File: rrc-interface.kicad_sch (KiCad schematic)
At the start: 39 parts, among them J1 Mic Input, J10 Input Only Pins, J11 Input Only Pins, J12 Flash mode, J2 8P8C_LED_Shielded, J3 6P6C RRC, J4 Audio Out, J5 Ptt, J6 TF Set, J7 UART2 Socket, J8 UART Socket, J9 SPI Breakout, U1 ESP32-DevKitC

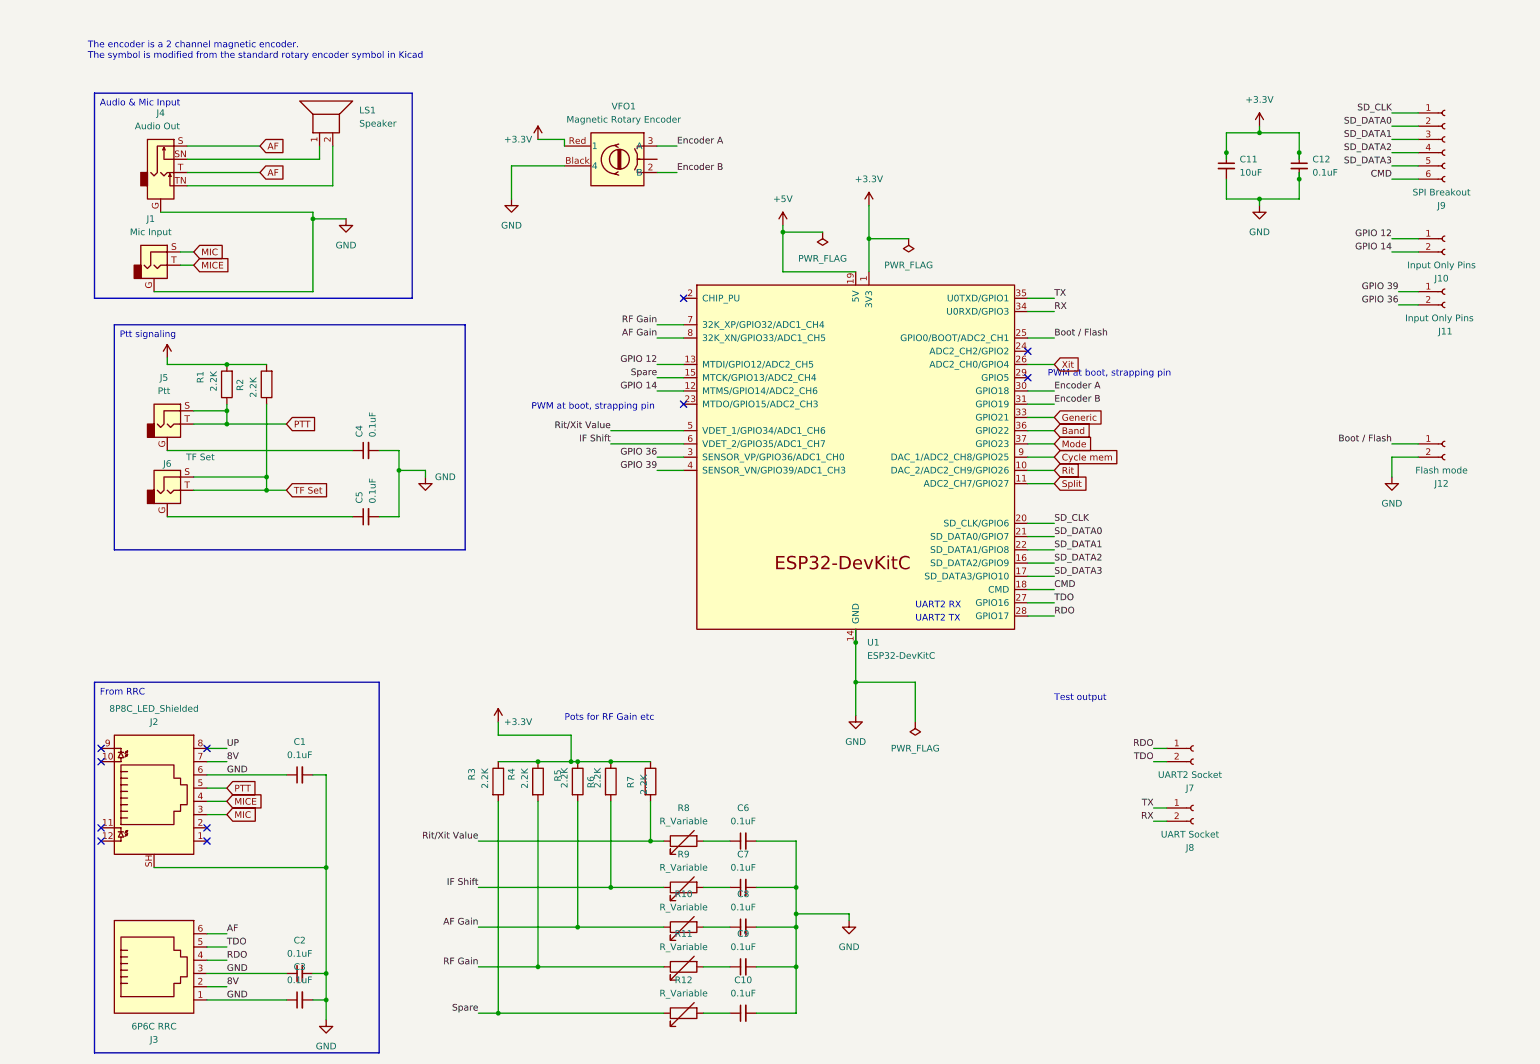
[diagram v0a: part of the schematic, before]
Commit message: cont routing work
Changes:

* Added mounting holes
* Tried to trim down PCB size a litle more.
* Attempted to separate digital IO from analog.
* Added socket IC for RJ45 & 6P6C / RJ12 configurability.
* WIP: Add muxer for UART line switching.

Comment:

The muxer UART functionality isn't complete, the idea is to allow switching between using
the RJ45 RXD & TXD UART to the RJ12 / 6P6C UART lines.
Since the real rrc hardware supports this (depends on the radio configured) & maybe depending on socket strapping..
Need to add a jumper to enable switching between these, alternatively use a GPIO pin??
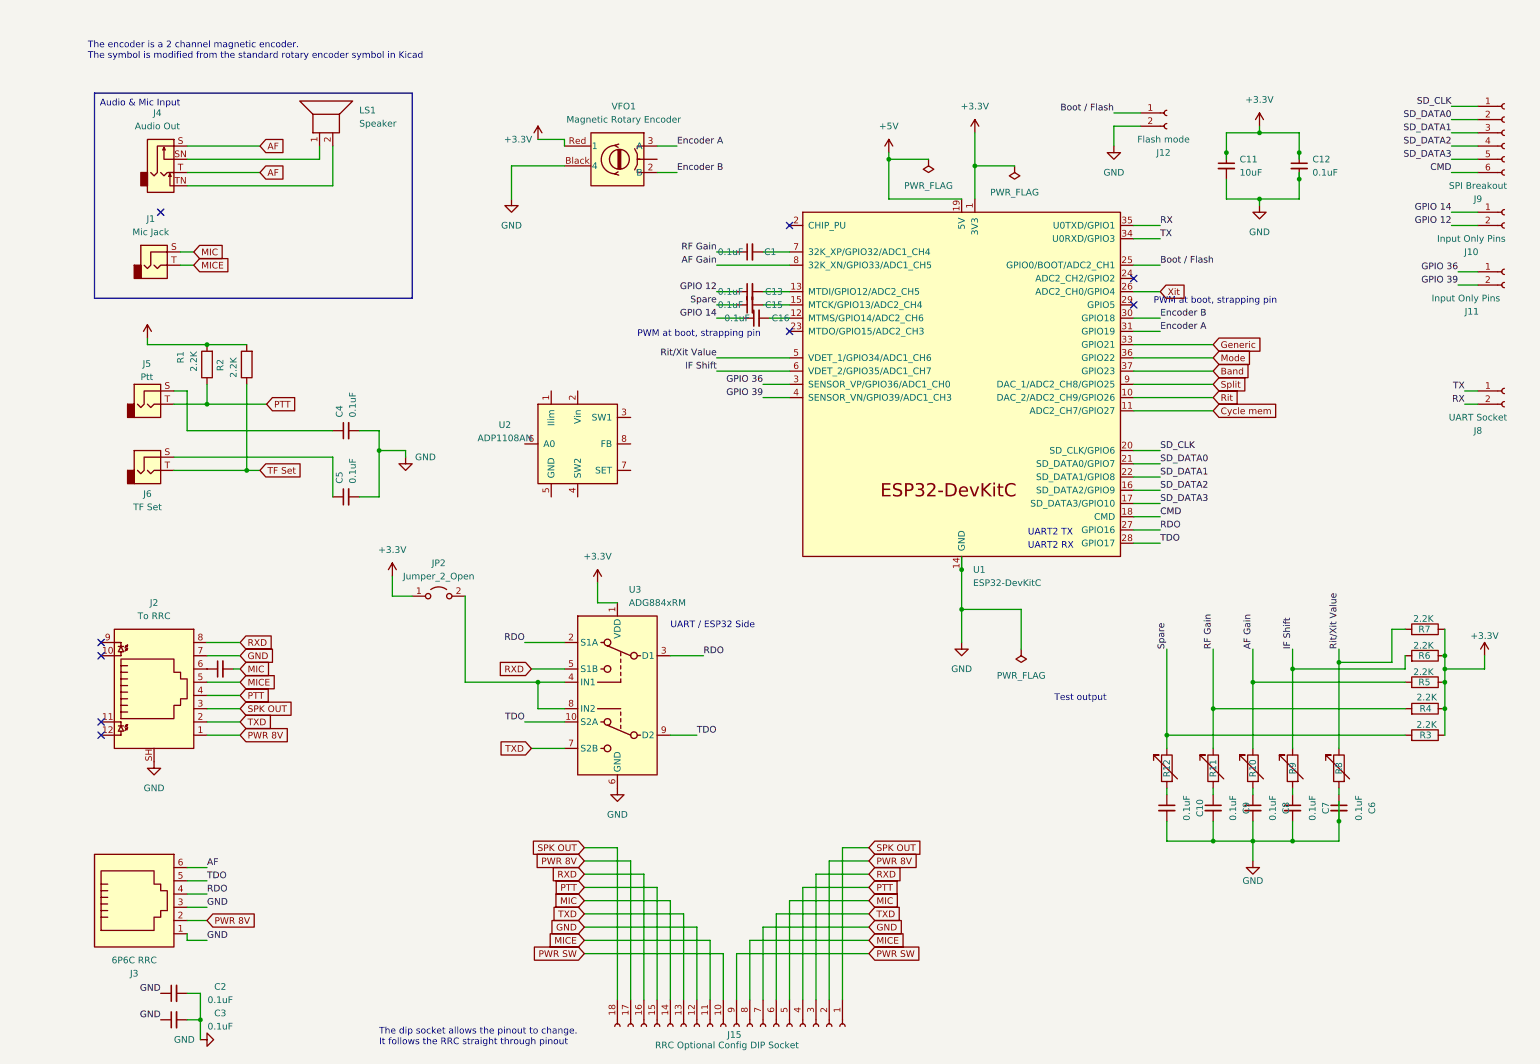
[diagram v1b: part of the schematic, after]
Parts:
- removed J1: Mic Input, Connector_Audio:Jack_3.5mm_CUI_SJ1-3533NG_Horizontal, symbol Connector_Audio:AudioJack2_Ground
- removed J4: Audio Out, Connector_Audio:Jack_3.5mm_CUI_SJ1-3535NG_Horizontal, symbol Connector_Audio:AudioJack2_Ground_Switch
- removed J5: Ptt, Connector_Audio:Jack_3.5mm_CUI_SJ1-3533NG_Horizontal, symbol Connector_Audio:AudioJack2_Ground
- removed J6: TF Set, Connector_Audio:Jack_3.5mm_CUI_SJ1-3533NG_Horizontal, symbol Connector_Audio:AudioJack2_Ground
- removed J7: UART2 Socket, Connector_Molex:Molex_KK-254_AE-6410-02A_1x02_P2.54mm_Vertical, symbol Connector:Conn_01x02_Socket
- added C13, C14, C15, C16: 0.1uF, Capacitor_SMD:C_0603_1608Metric, symbol Device:C_Small
- added J1: Mic Jack, Connector_Audio:Jack_3.5mm_CUI_SJ1-3523N_Horizontal, symbol Connector_Audio:AudioJack2
- added J15: RRC Optional Config DIP Socket, Package_DIP:DIP-18_W7.62mm_Socket, symbol Connector:Conn_01x18_Socket
- added J4: Audio Out, Connector_Audio:Jack_3.5mm_CUI_SJ1-3535NG_Horizontal, symbol Connector_Audio:AudioJack2_Switch
- added J5: Ptt, Connector_Audio:Jack_3.5mm_CUI_SJ1-3523N_Horizontal, symbol Connector_Audio:AudioJack2
- added J6: TF Set, Connector_Audio:Jack_3.5mm_CUI_SJ1-3523N_Horizontal, symbol Connector_Audio:AudioJack2
- added JP2: Jumper_2_Open, symbol Jumper:Jumper_2_Open
- added U2: ADP1108AN, Package_DIP:DIP-8_W7.62mm, symbol Regulator_Switching:ADP1108AN
- added U3: ADG884xRM, Package_SO:MSOP-10_3x3mm_P0.5mm, symbol Analog_Switch:ADG884xRM
- J2: value 8P8C_LED_Shielded -> To RRC
- J9: footprint Connector_Molex:Molex_KK-254_AE-6410-06A_1x06_P2.54mm_Vertical -> Connector_PinSocket_2.54mm:PinSocket_1x06_P2.54mm_Vertical
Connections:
- net +3V3: now also JP2.1 (A), U3.1 (VDD)
- net AF: now also J4.S, J4.T
- net Band: now also U1.37 (GPIO23); no longer U1.36 (GPIO22)
- net Cycle mem: now also U1.11 (ADC2_CH7/GPIO27); no longer U1.9 (DAC_1/ADC2_CH8/GPIO25)
- net Encoder A: now also U1.31 (GPIO19); no longer U1.30 (GPIO18)
- net Encoder B: now also U1.30 (GPIO18); no longer U1.31 (GPIO19)
- net GND: now also J2.7, J15.12 (GND), J15.7 (GND), U3.6 (GND); no longer C1.1, C1.2, J2.6
- net GPIO 12: now also J10.2 (Pin_2), C13.1; no longer J10.1 (Pin_1), U1.13 (MTDI/GPIO12/ADC2_CH5)
- net GPIO 14: now also J10.1 (Pin_1), C16.1; no longer J10.2 (Pin_2), U1.12 (MTMS/GPIO14/ADC2_CH6)
- net GPIO 36: now also J11.1 (Pin_1); no longer J11.2 (Pin_2)
- net GPIO 39: now also J11.2 (Pin_2); no longer J11.1 (Pin_1)
- net MIC: now also C14.2, J1.S, J15.14 (MIC), J15.5 (MIC); no longer J2.3
- net MICE: now also J2.5, J1.T, J15.11 (MICE), J15.8 (MICE); no longer J2.4
- net Mode: now also U1.36 (GPIO22); no longer U1.37 (GPIO23)
- net PTT: now also J2.4, J15.15 (PWR_ON_SW), J15.4 (PWR_ON_SW), J5.T; no longer J2.5
- net RDO: now also U1.27 (GPIO16), U3.2 (S1A), U3.3 (D1); no longer U1.28 (GPIO17)
- net RF Gain: now also C1.1; no longer U1.7 (32K_XP/GPIO32/ADC1_CH4)
- net RX: now also U1.35 (U0TXD/GPIO1); no longer U1.34 (U0RXD/GPIO3)
- net Spare: now also C15.1; no longer U1.15 (MTCK/GPIO13/ADC2_CH4)
- net Split: now also U1.9 (DAC_1/ADC2_CH8/GPIO25); no longer U1.11 (ADC2_CH7/GPIO27)
- net TDO: now also U1.28 (GPIO17), U3.10 (S2A), U3.9 (D2); no longer U1.27 (GPIO16)
- net TF Set: now also J6.T
- net TX: now also U1.34 (U0RXD/GPIO3); no longer U1.35 (U0TXD/GPIO1)
- net at C4.1: now also J5.S
- net PWR 8V: now reaches J2.1
- net PWR 8V: now also J3.2, J15.17 (PWR_(8/9V)), J15.2 (PWR_(8/9V))
- net TXD: now reaches J2.2
- net TXD: now also J15.13 (TXD), J15.6 (TXD), U3.7 (S2B)
- net at LS1.1: now also J4.SN
- net at LS1.2: now also J4.TN
- net at C5.1: now also J6.S
- removed net 8V: J2.7, J3.2
- net UP renamed RXD
- net RXD: now also J15.16 (RXD), J15.3 (RXD), U3.5 (S1B)
- new net: C13.2, U1.13 (MTDI/GPIO12/ADC2_CH5)
- new net: C1.2, U1.7 (32K_XP/GPIO32/ADC1_CH4)
- new net: C14.1, J2.6
- new net: C16.2, U1.12 (MTMS/GPIO14/ADC2_CH6)
- new net: JP2.2 (B), U3.4 (IN1), U3.8 (IN2)
- new net: C15.2, U1.15 (MTCK/GPIO13/ADC2_CH4)
- new net PWR SW: J15.10 (NC), J15.9 (NC)
- new net SPK OUT: J15.1 (SPK_OUT), J15.18 (SPK_OUT), J2.3
- no-connect marks 11 -> 9
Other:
- note added: "The dip socket allows the pinout to change. It follows the RRC straight through pinout"
- note added: "UART / ESP32 Side"
- note removed: "Pots for RF Gain etc"
- moved on the sheet: C10, C2, C3, C4, C5, C6, C7, C8, C9, J10, J11, J12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

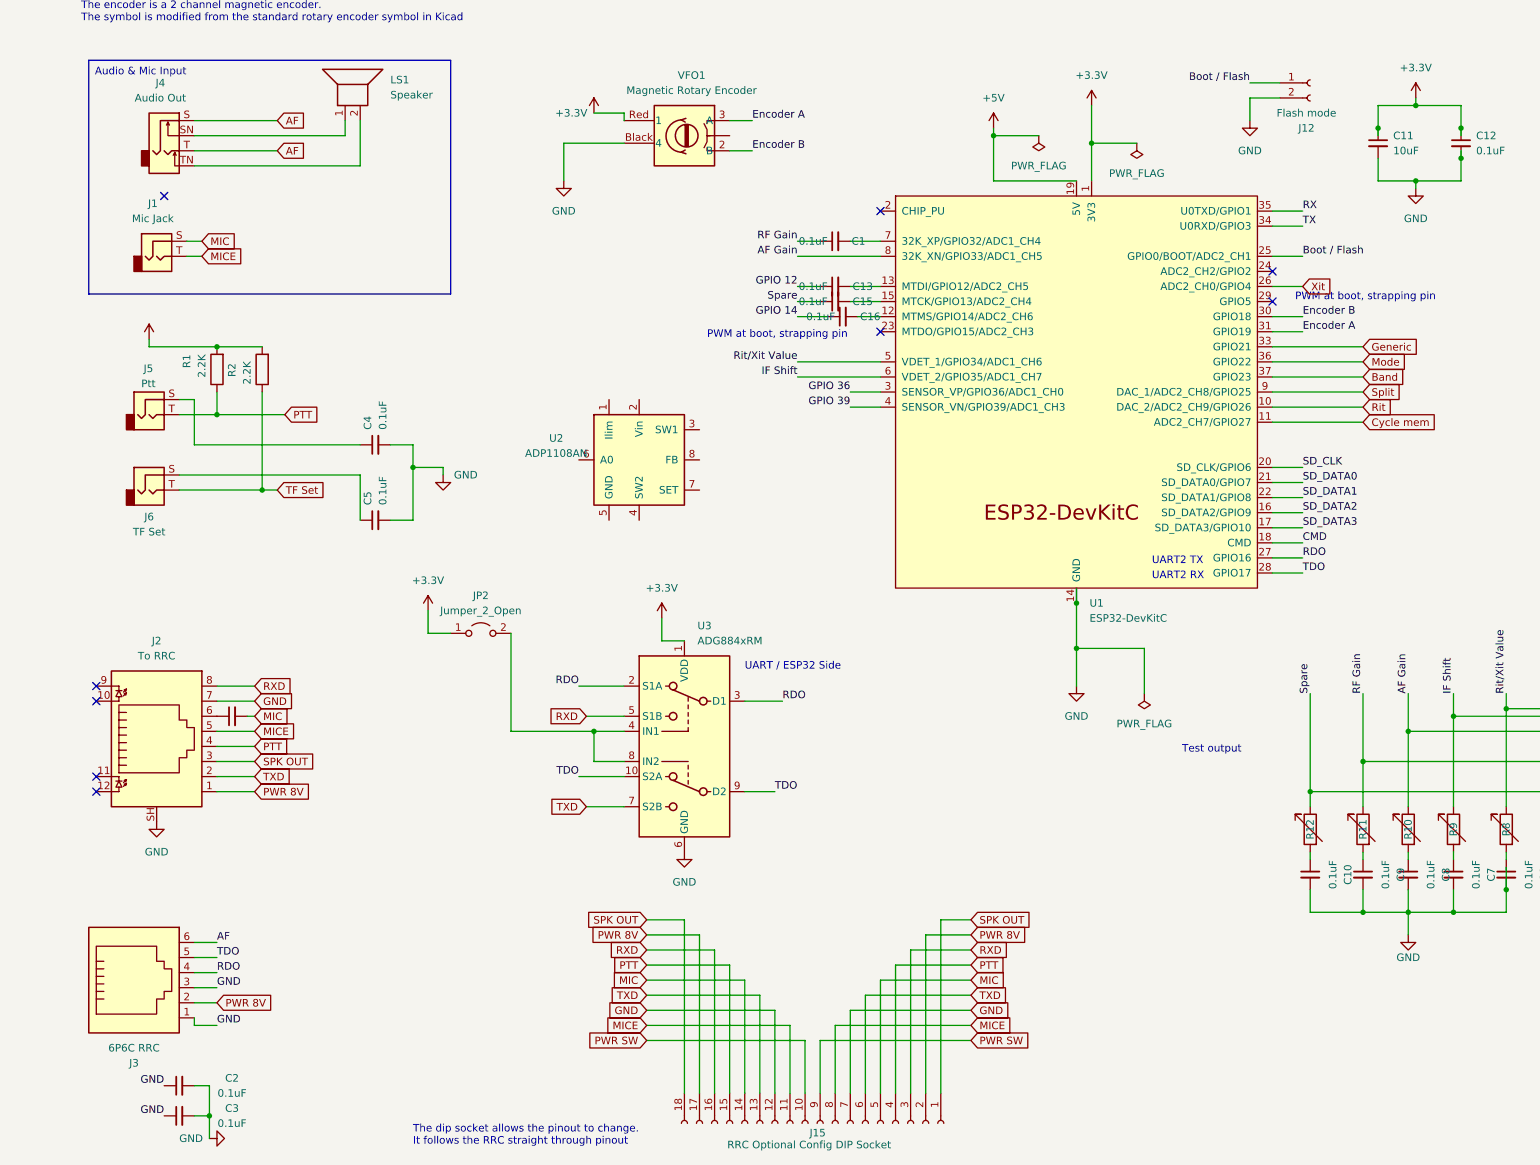
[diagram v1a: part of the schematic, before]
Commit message: add gnd pour to top layer, try to optimize routing
Changes:

* Opt to use normal via's instead of micro via's to reduce cost / production time.
* Add ground pour / plane to top layer.
* Reorganize component layout a bit to try to optimize paths.
* Change connector types to JST (will soon have a crimp kit for these connectors).
* Try to split the PCB into analog and digital sections.
* Add mounting holes.
* Increase track size for power traces.

TODO:

* Via stitching to make sure the resistance between planes is as low as possible?
* Configure board size.
* Finish variable resistor PCB's & add connectors to the PCB's for interconnect.
* Remove 3.5mm jacks from layout, need separate PCB's for these. Need to be able to mount the jack's on a panel, need flexibility.
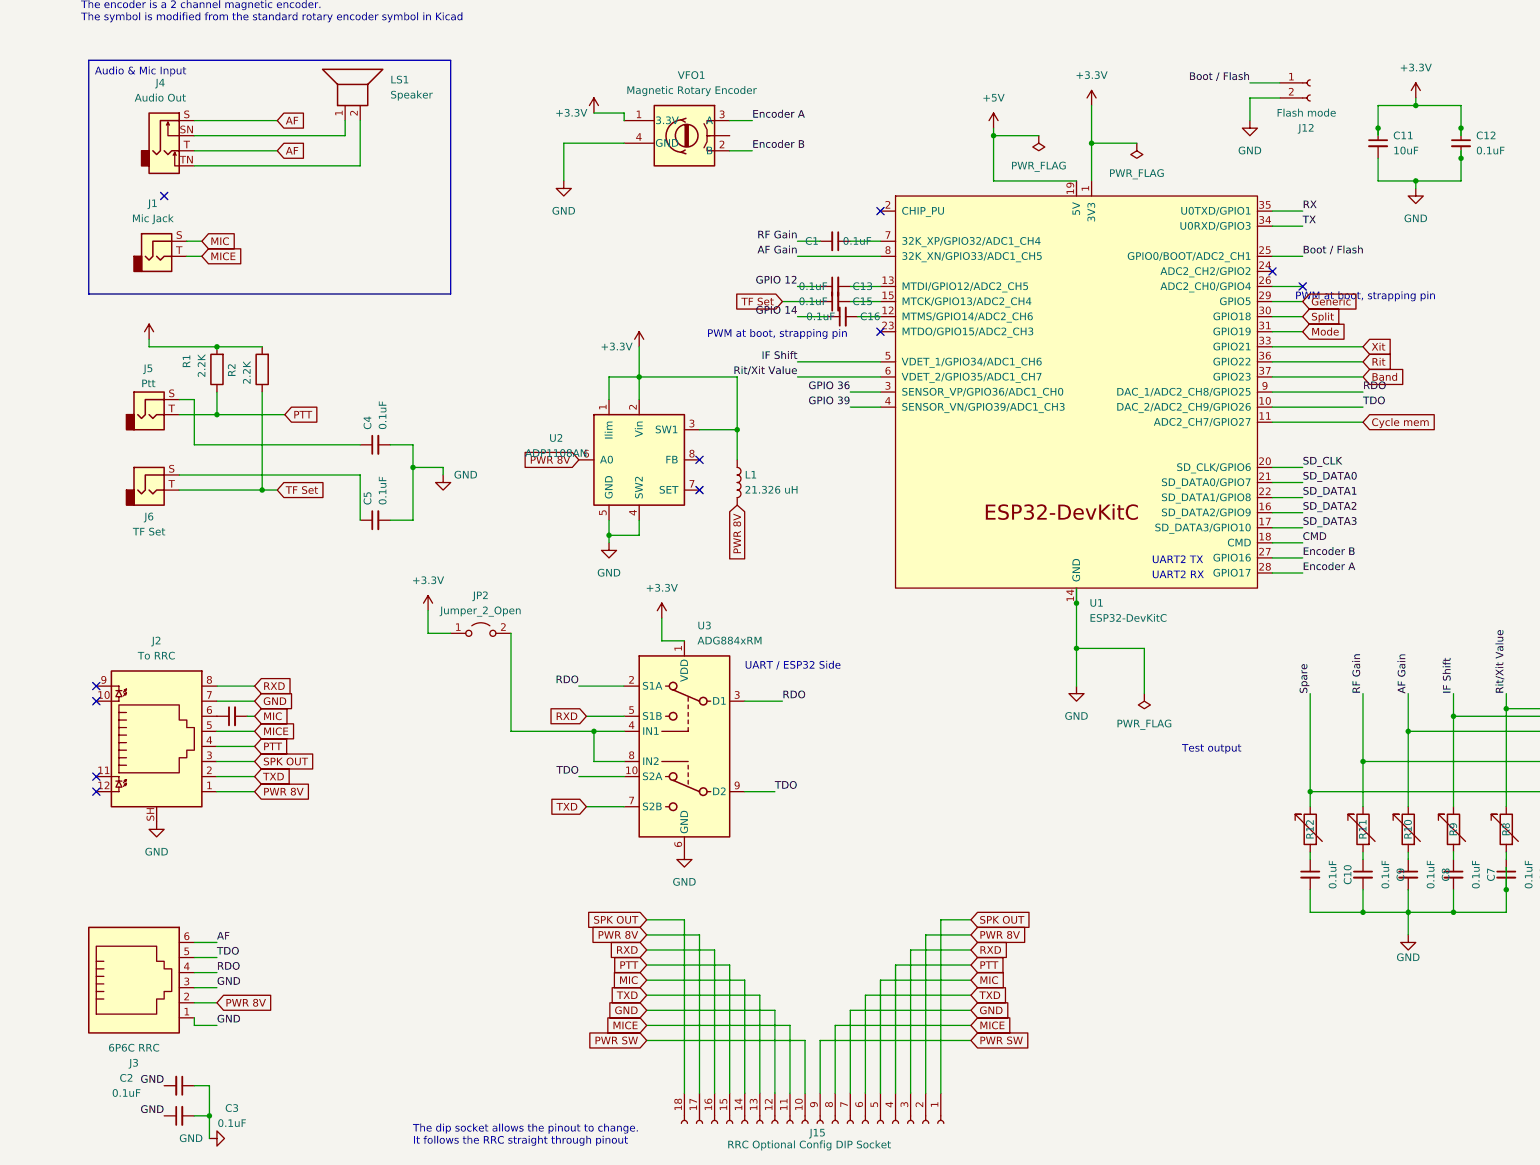
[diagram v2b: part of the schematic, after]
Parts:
- added L1: 21.326 uH, symbol Device:L
- J10, J11, J8: footprint Connector_Molex:Molex_KK-254_AE-6410-02A_1x02_P2.54mm_Vertical -> Connector_JST:JST_PH_B2B-PH-K_1x02_P2.00mm_Vertical
- R10, R11, R12, R8, R9: footprint Connector_Molex:Molex_KK-254_AE-6410-06A_1x06_P2.54mm_Vertical -> Connector_JST:JST_PH_B2B-PH-K_1x02_P2.00mm_Vertical
- VFO1: footprint Connector_Molex:Molex_KK-254_AE-6410-04A_1x04_P2.54mm_Vertical -> Connector_JST:JST_PH_B4B-PH-K_1x04_P2.00mm_Vertical
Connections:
- net +3V3: now also U2.1 (Ilim), U2.2 (Vin), U2.3 (SW1), VFO1.1 (3.3V), L1.1; no longer VFO1.Red (1)
- net Encoder A: now also U1.28 (GPIO17); no longer U1.31 (GPIO19)
- net Encoder B: now also U1.27 (GPIO16); no longer U1.30 (GPIO18)
- net GND: now also U2.4 (SW2), U2.5 (GND), VFO1.4 (GND); no longer VFO1.Black (4)
- net Generic: now also U1.29 (GPIO5); no longer U1.33 (GPIO21)
- net IF Shift: now also U1.5 (VDET_1/GPIO34/ADC1_CH6); no longer U1.6 (VDET_2/GPIO35/ADC1_CH7)
- net Mode: now also U1.31 (GPIO19); no longer U1.36 (GPIO22)
- net PWR 8V: now also U2.6 (A0), L1.2
- net RDO: now also U1.9 (DAC_1/ADC2_CH8/GPIO25); no longer U1.27 (GPIO16)
- net RF Gain: now also C1.2; no longer C1.1
- net Rit: now also U1.36 (GPIO22); no longer U1.10 (DAC_2/ADC2_CH9/GPIO26)
- net Rit/Xit Value: now also U1.6 (VDET_2/GPIO35/ADC1_CH7); no longer U1.5 (VDET_1/GPIO34/ADC1_CH6)
- net Spare: no longer C15.1
- net Split: now also U1.30 (GPIO18); no longer U1.9 (DAC_1/ADC2_CH8/GPIO25)
- net TDO: now also U1.10 (DAC_2/ADC2_CH9/GPIO26); no longer U1.28 (GPIO17)
- net TF Set: now also C15.1
- net Xit: now also U1.33 (GPIO21); no longer U1.26 (ADC2_CH0/GPIO4)
- net at U1.7 (32K_XP/GPIO32/ADC1_CH4): now also C1.1; no longer C1.2
- no-connect marks 9 -> 11
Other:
- moved on the sheet: C1, C2
